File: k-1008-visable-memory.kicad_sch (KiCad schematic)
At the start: 2 parts, among them J1 Video Out, J2 EDGE_CONN

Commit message: Various corrections. Add new symbols and footprints
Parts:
- J1: footprint (none) -> K-1008:RCA_Horizontal
- J2: footprint KIM-1_Library:KIM_CONN -> K-1008:EDGE_CONN
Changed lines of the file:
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@@
       (effects (font (size 1.27 1.27)))
     )
-    (property "Footprint" "KIM-1_Library:KIM_CONN" (at 52.959 132.588 0)
+    (property "Footprint" "K-1008:EDGE_CONN" (at 52.959 132.588 0)
       (effects (font (size 1.27 1.27)) hide)
     )
@@
       (effects (font (size 1.27 1.27)) (justify right))
     )
-    (property "Footprint" "" (at 273.558 22.606 0)
+    (property "Footprint" "K-1008:RCA_Horizontal" (at 273.558 22.606 0)
       (effects (font (size 1.27 1.27)) hide)
     )

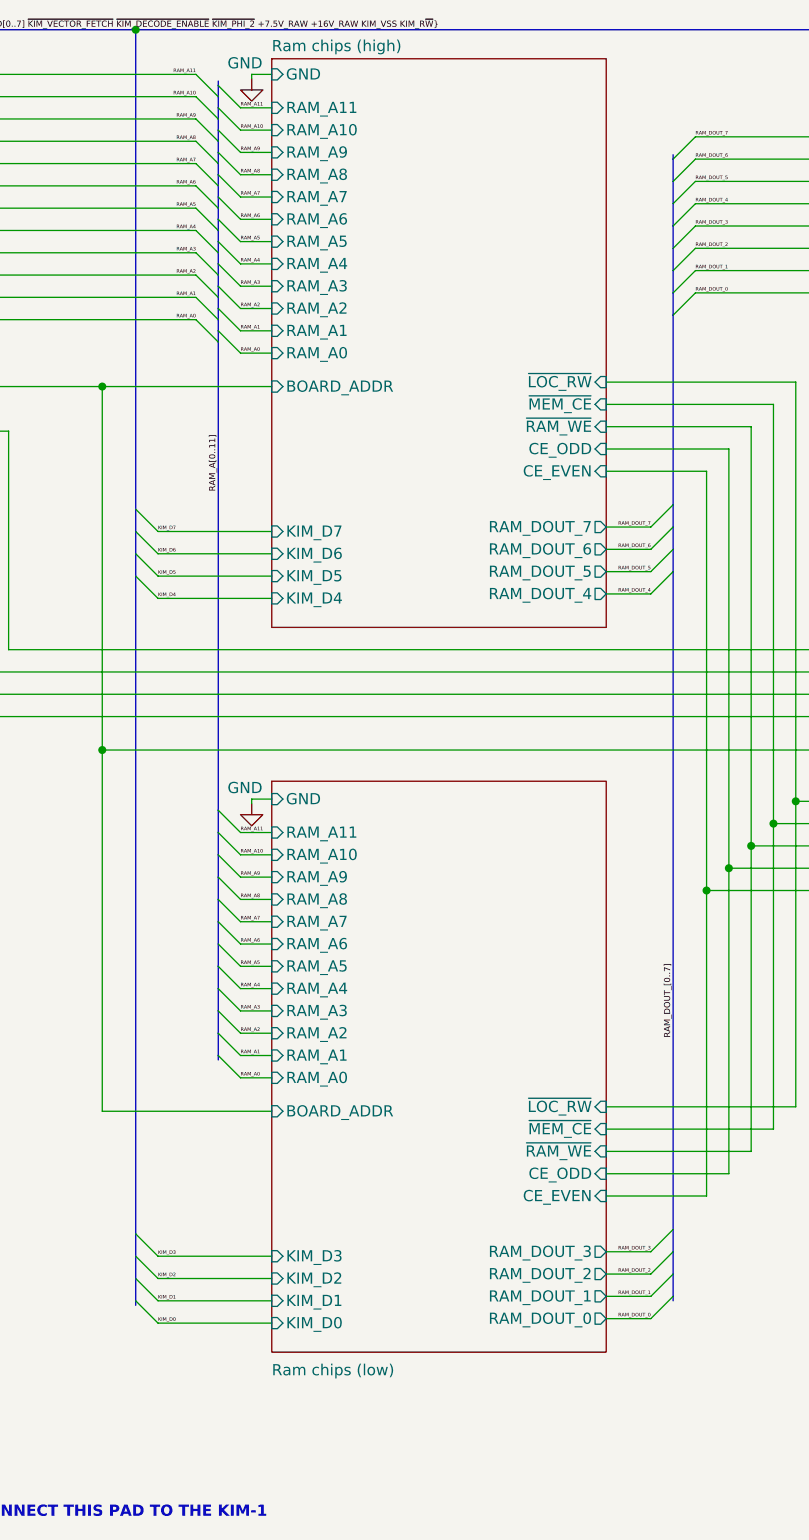
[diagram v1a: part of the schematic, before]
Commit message: Swap high and low RAM nibbles
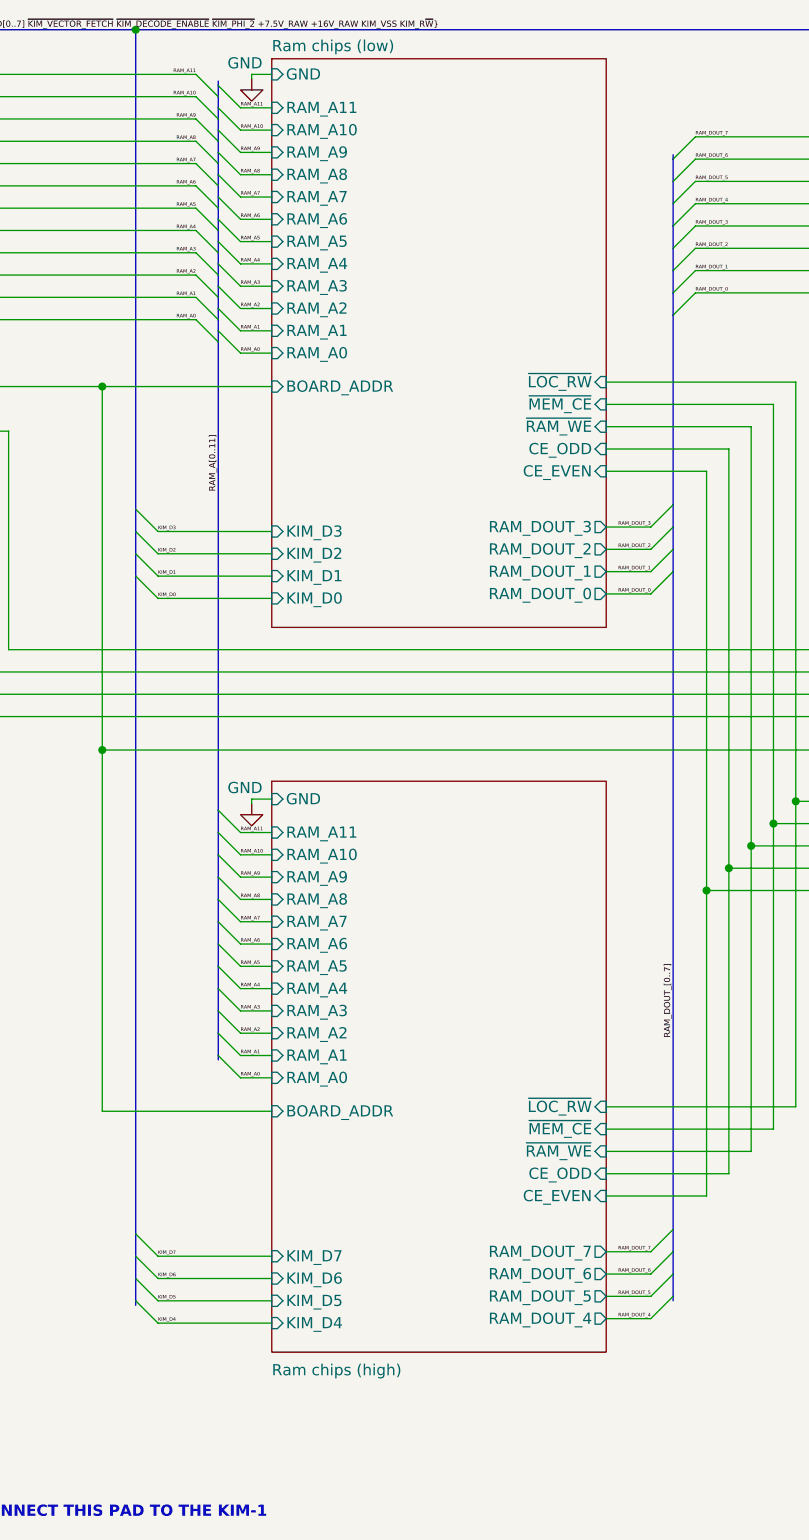
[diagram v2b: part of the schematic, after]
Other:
- sheet Ram chips (high): file Ram_chips_high.kicad_sch -> Ram_chips_low.kicad_sch
- sheet Ram chips (low): file Ram_chips_low.kicad_sch -> Ram_chips_high.kicad_sch
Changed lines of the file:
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@@
     (effects (font (size 0.4 0.4)) (justify left bottom))
   )
-  (label "KIM_D4" (at 109.22 81.788 0) (fields_autoplaced)
+  (label "KIM_D0" (at 109.22 81.788 0) (fields_autoplaced)
     (effects (font (size 0.4 0.4)) (justify left bottom))
   )
@@
     (effects (font (size 0.4 0.4)) (justify left bottom))
   )
-  (label "KIM_D2" (at 109.22 159.258 0) (fields_autoplaced)
+  (label "KIM_D6" (at 109.22 159.258 0) (fields_autoplaced)
     (effects (font (size 0.4 0.4)) (justify left bottom))
   )
@@
     (effects (font (size 0.4 0.4)) (justify left bottom))
   )
-  (label "KIM_D3" (at 109.22 156.718 0) (fields_autoplaced)
+  (label "KIM_D7" (at 109.22 156.718 0) (fields_autoplaced)
     (effects (font (size 0.4 0.4)) (justify left bottom))
   )
@@
     (effects (font (size 0.4 0.4)) (justify left bottom))
   )
-  (label "KIM_D5" (at 109.22 79.248 0) (fields_autoplaced)
+  (label "KIM_D1" (at 109.22 79.248 0) (fields_autoplaced)
     (effects (font (size 0.4 0.4)) (justify left bottom))
   )
@@
     (effects (font (size 0.4 0.4)) (justify left bottom))
   )
-  (label "KIM_D1" (at 109.22 161.798 0) (fields_autoplaced)
-    (effects (font (size 0.4 0.4)) (justify left bottom))
-  )
-  (label "RAM_DOUT_5" (at 165.354 78.74 180) (fields_autoplaced)
-    (effects (font (size 0.4 0.4)) (justify right bottom))
-  )
-  (label "RAM_DOUT_1" (at 165.354 161.29 180) (fields_autoplaced)
+  (label "KIM_D5" (at 109.22 161.798 0) (fields_autoplaced)
+    (effects (font (size 0.4 0.4)) (justify left bottom))
+  )
+  (label "RAM_DOUT_1" (at 165.354 78.74 180) (fields_autoplaced)
+    (effects (font (size 0.4 0.4)) (justify right bottom))
+  )
+  (label "RAM_DOUT_5" (at 165.354 161.29 180) (fields_autoplaced)
     (effects (font (size 0.4 0.4)) (justify right bottom))
   )
@@
     (effects (font (size 0.7 0.7)) (justify left bottom))
   )
-  (label "RAM_DOUT_3" (at 165.354 156.21 180) (fields_autoplaced)
+  (label "RAM_DOUT_7" (at 165.354 156.21 180) (fields_autoplaced)
     (effects (font (size 0.4 0.4)) (justify right bottom))
   )
@@
     (effects (font (size 0.4 0.4)) (justify left bottom))
   )
-  (label "RAM_DOUT_7" (at 165.354 73.66 180) (fields_autoplaced)
+  (label "RAM_DOUT_3" (at 165.354 73.66 180) (fields_autoplaced)
     (effects (font (size 0.4 0.4)) (justify right bottom))
   )
@@
     (effects (font (size 0.4 0.4)) (justify left bottom))
   )
-  (label "RAM_DOUT_6" (at 165.354 76.2 180) (fields_autoplaced)
+  (label "RAM_DOUT_2" (at 165.354 76.2 180) (fields_autoplaced)
     (effects (font (size 0.4 0.4)) (justify right bottom))
   )
@@
     (effects (font (size 0.4 0.4)) (justify left bottom))
   )
-  (label "RAM_DOUT_4" (at 165.354 81.28 180) (fields_autoplaced)
+  (label "RAM_DOUT_0" (at 165.354 81.28 180) (fields_autoplaced)
     (effects (font (size 0.4 0.4)) (justify right bottom))
   )
@@
     (effects (font (size 0.4 0.4)) (justify left bottom))
   )
-  (label "RAM_DOUT_2" (at 165.354 158.75 180) (fields_autoplaced)
+  (label "RAM_DOUT_6" (at 165.354 158.75 180) (fields_autoplaced)
     (effects (font (size 0.4 0.4)) (justify right bottom))
   )
@@
     (effects (font (size 0.4 0.4)) (justify left bottom))
   )
-  (label "KIM_D7" (at 109.22 74.168 0) (fields_autoplaced)
+  (label "KIM_D3" (at 109.22 74.168 0) (fields_autoplaced)
     (effects (font (size 0.4 0.4)) (justify left bottom))
   )
@@
     (effects (font (size 0.4 0.4)) (justify left bottom))
   )
-  (label "KIM_D6" (at 109.22 76.708 0) (fields_autoplaced)
-    (effects (font (size 0.4 0.4)) (justify left bottom))
-  )
-  (label "RAM_DOUT_0" (at 165.354 163.83 180) (fields_autoplaced)
+  (label "KIM_D2" (at 109.22 76.708 0) (fields_autoplaced)
+    (effects (font (size 0.4 0.4)) (justify left bottom))
+  )
+  (label "RAM_DOUT_4" (at 165.354 163.83 180) (fields_autoplaced)
     (effects (font (size 0.4 0.4)) (justify right bottom))
   )
@@
     (effects (font (size 0.4 0.4)) (justify left bottom))
   )
-  (label "KIM_D0" (at 109.22 164.338 0) (fields_autoplaced)
+  (label "KIM_D4" (at 109.22 164.338 0) (fields_autoplaced)
     (effects (font (size 0.4 0.4)) (justify left bottom))
   )
@@
     (stroke (width 0.1524) (type solid))
     (fill (color 255 153 0 0.3000))
-    (property "Sheetname" "Ram chips (high)" (at 122.174 19.6084 0)
+    (property "Sheetname" "Ram chips (low)" (at 122.174 19.6084 0)
       (effects (font (size 1.27 1.27)) (justify left bottom))
     )
@@
       (effects (font (size 1.27 1.27)) (justify right))
     )
-    (pin "KIM_D6" input (at 122.174 76.708 180)
-      (effects (font (size 1.27 1.27)) (justify left))
-    )
-    (pin "KIM_D7" input (at 122.174 74.168 180)
+    (pin "KIM_D2" input (at 122.174 76.708 180)
+      (effects (font (size 1.27 1.27)) (justify left))
+    )
+    (pin "KIM_D3" input (at 122.174 74.168 180)
       (effects (font (size 1.27 1.27)) (justify left))
     )
@@
       (effects (font (size 1.27 1.27)) (justify right))
     )
-    (pin "KIM_D4" input (at 122.174 81.788 180)
-      (effects (font (size 1.27 1.27)) (justify left))
-    )
-    (pin "KIM_D5" input (at 122.174 79.248 180)
+    (pin "KIM_D0" input (at 122.174 81.788 180)
+      (effects (font (size 1.27 1.27)) (justify left))
+    )
+    (pin "KIM_D1" input (at 122.174 79.248 180)
       (effects (font (size 1.27 1.27)) (justify left))
     )
@@
       (effects (font (size 1.27 1.27)) (justify left))
     )
-    (pin "RAM_DOUT_4" output (at 160.274 81.28 0)
-      (effects (font (size 1.27 1.27)) (justify right))
-    )
-    (pin "RAM_DOUT_5" output (at 160.274 78.74 0)
-      (effects (font (size 1.27 1.27)) (justify right))
-    )
-    (pin "RAM_DOUT_6" output (at 160.274 76.2 0)
-      (effects (font (size 1.27 1.27)) (justify right))
-    )
-    (pin "RAM_DOUT_7" output (at 160.274 73.66 0)
+    (pin "RAM_DOUT_0" output (at 160.274 81.28 0)
+      (effects (font (size 1.27 1.27)) (justify right))
+    )
+    (pin "RAM_DOUT_1" output (at 160.274 78.74 0)
+      (effects (font (size 1.27 1.27)) (justify right))
+    )
+    (pin "RAM_DOUT_2" output (at 160.274 76.2 0)
+      (effects (font (size 1.27 1.27)) (justify right))
+    )
+    (pin "RAM_DOUT_3" output (at 160.274 73.66 0)
       (effects (font (size 1.27 1.27)) (justify right))
     )
@@
     (stroke (width 0.1524) (type solid))
     (fill (color 128 77 0 0.3000))
-    (property "Sheetname" "Ram chips (low)" (at 122.174 170.434 0)
+    (property "Sheetname" "Ram chips (high)" (at 122.174 170.434 0)
       (effects (font (size 1.27 1.27)) (justify left bottom))
     )
@@
       (effects (font (size 1.27 1.27)) (justify left))
     )
-    (pin "RAM_DOUT_3" output (at 160.274 156.21 0)
-      (effects (font (size 1.27 1.27)) (justify right))
-    )
-    (pin "RAM_DOUT_2" output (at 160.274 158.75 0)
-      (effects (font (size 1.27 1.27)) (justify right))
-    )
-    (pin "RAM_DOUT_1" output (at 160.274 161.29 0)
-      (effects (font (size 1.27 1.27)) (justify right))
-    )
-    (pin "RAM_DOUT_0" output (at 160.274 163.83 0)
-      (effects (font (size 1.27 1.27)) (justify right))
-    )
-    (pin "KIM_D2" input (at 122.174 159.258 180)
-      (effects (font (size 1.27 1.27)) (justify left))
-    )
-    (pin "KIM_D3" input (at 122.174 156.718 180)
-      (effects (font (size 1.27 1.27)) (justify left))
-    )
-    (pin "KIM_D1" input (at 122.174 161.798 180)
-      (effects (font (size 1.27 1.27)) (justify left))
-    )
-    (pin "KIM_D0" input (at 122.174 164.338 180)
-      (effects (font (size 1.27 1.27)) (justify left))
-    )
+    (pin "RAM_DOUT_7" output (at 160.274 156.21 0)
+      (effects (font (size 1.27 1.27)) (justify right))
+    )
+    (pin "RAM_DOUT_6" output (at 160.274 158.75 0)
+      (effects (font (size 1.27 1.27)) (justify right))
+    )
+    (pin "RAM_DOUT_5" output (at 160.274 161.29 0)
+      (effects (font (size 1.27 1.27)) (justify right))
+    )
+    (pin "RAM_DOUT_4" output (at 160.274 163.83 0)
+      (effects (font (size 1.27 1.27)) (justify right))
+    )
+    (pin "KIM_D6" input (at 122.174 159.258 180)
+      (effects (font (size 1.27 1.27)) (justify left))
+    )
+    (pin "KIM_D7" input (at 122.174 156.718 180)
+      (effects (font (size 1.27 1.27)) (justify left))
+    )
+    (pin "KIM_D5" input (at 122.174 161.798 180)
+      (effects (font (size 1.27 1.27)) (justify left))
+    )
+    (pin "KIM_D4" input (at 122.174 164.338 180)
+      (effects (font (size 1.27 1.27)) (justify left))
+    )
